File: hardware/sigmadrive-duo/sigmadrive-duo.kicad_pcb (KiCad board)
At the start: 4 copper layers, 100 x 104 mm, 192 parts, among them J10 Conn_01x03, J11 Conn_01x03, J12 Conn_02x05_Odd_Even, J2 CONN_02X05, J4 Conn_01x05, J6 629_105_150_921, J8 Conn_01x03, J9 Conn_01x03, M1 Conn_01x04, M2 Conn_01x04, Q1 NTMFS5C628NLT1G, Q10 NTMFS5C628NLT1G, Q11 NTMFS5C628NLT1G, Q12 NTMFS5C628NLT1G, Q2 NTMFS5C628NLT1G, Q3 NTMFS5C628NLT1G, Q4 NTMFS5C628NLT1G, Q5 NTMFS5C628NLT1G, Q6 NTMFS5C628NLT1G, Q7 NTMFS5C628NLT1G, Q8 NTMFS5C628NLT1G, Q9 NTMFS5C628NLT1G, SW1 SW_DIP_x04, SW2 SW_DIP_x04, U1 DRV8323RS, U12 SN65HVD75DGKR, U2 DRV8323RS, U3 SN65HVD75DGKR, U4 TPD4S009, U5 STM32F745VGTx, U6 TPD4S009, U7 TPS70933, Y1 NX3225SA-12.000M-STD-CSR-1

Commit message: Work on duo drive.
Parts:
- removed R11, R12: 21, Resistor_SMD:R_0603_1608Metric
- removed R6: 10k, Resistor_SMD:R_0603_1608Metric
- removed SW1: SW_DIP_x04, Button_Switch_SMD:SW_DIP_SPSTx04_Slide_Copal_CHS-04A_W5.08mm_P1.27mm_JPin
- added C4: 100nF 50V, Capacitor_SMD:C_0603_1608Metric, F.Cu at (73.2, 104.8)
- added J1: Conn_02x05_Odd_Even, Connector_PinHeader_2.00mm:PinHeader_2x05_P2.00mm_Horizontal, F.Cu at (66.9, 105.0)
- added R10: 10k, Resistor_SMD:R_0603_1608Metric, F.Cu at (70.4, 93.3)
- added R25: 10k, Resistor_SMD:R_0603_1608Metric, F.Cu at (174.6, 93.0)
- added R33: 10k, Resistor_SMD:R_0603_1608Metric, F.Cu at (171.0, 119.9)
- added R48: 10k, Resistor_SMD:R_0603_1608Metric, F.Cu at (182.8, 122.2)
- added R9: 10k, Resistor_SMD:R_0603_1608Metric, F.Cu at (72.6, 93.3)
- added U8: SN65HVD75DGKR, Package_SO:SOIC-8_3.9x4.9mm_P1.27mm, F.Cu at (71.2, 99.2)
- C5, R14, R15, U3: moved to F.Cu
- moved R44 106.4 mm to (136.5, 65.1)
- moved R2 95.5 mm to (121.0, 64.7)
- moved R3 95.5 mm to (122.5, 64.7)
- moved R5 95.5 mm to (124.0, 64.7)
- moved R24 92.5 mm to (106.6, 105.3), turned to 90 degrees
- moved C45 91.1 mm to (103.6, 105.3), turned to 270 degrees
- moved R23 90.3 mm to (108.1, 105.3), turned to 90 degrees
- moved R34 89.7 mm to (105.1, 105.3), turned to 270 degrees
- moved R19 69.5 mm to (98.3, 73.9), turned to 180 degrees
- moved J2 63.1 mm to (126.7, 59.6)
- moved R8 58.2 mm to (127.0, 64.7), turned to 90 degrees
- moved C3 56.9 mm to (125.5, 64.7), turned to 270 degrees
- moved J12 52.9 mm to (148.1, 97.0)
- moved R36 41.3 mm to (221.2, 130.3)
- moved RV2 41.3 mm to (225.8, 130.3)
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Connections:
- C51 pad 2: /MCU/PB14 -> /MCU/SW1
- C52 pad 2: /MCU/PB15 -> /MCU/SW2
- J4 pad 3: /MCU/PB4 -> /MCU/PWM_IN
- J8 pad 3: /MCU/PB14 -> /MCU/SW1
- J9 pad 3: /MCU/PB15 -> /MCU/SW2
- R17 pad 2: /MCU/PB14 -> /MCU/SW1
- R28 pad 2: /MCU/PB15 -> /MCU/SW2
- R36 pad 2: /MCU/PA4 -> /MCU/PC4
- R84 pad 2: /MCU/PD6 -> /MCU/PC11
- R85 pad 1: /MCU/PD4 -> /MCU/PA15
- RV2 pad 2: /MCU/PA4 -> /MCU/PC4
- SW2 pad 2: +3V3 -> GND
- SW2 pad 3: GND -> +3V3
- SW2 pad 5: /MCU/GPIO_CONF_4 -> /MCU/BOOT0
- U1 pad 29: Net-(R12-Pad2) -> /MCU/DRV_SDO
- U12 pad 1: /MCU/PD6 -> /MCU/PC11
- U12 pad 2: /MCU/PD4 -> /MCU/PA15
- U12 pad 3: /MCU/PD4 -> /MCU/PA15
- U12 pad 4: /MCU/PD5 -> /MCU/PC10
- U2 pad 29: Net-(R11-Pad2) -> /MCU/DRV_SDO
- U3 pad 6: Net-(J12-Pad7) -> Net-(J12-Pad5)
- U3 pad 7: Net-(J12-Pad5) -> Net-(J12-Pad7)
- U5 pad 1: /MCU/GPIO_CONF_3 -> /MCU/PE2
- U5 pad 2: /MCU/GPIO_CONF_4 -> /MCU/PE3
- U5 pad 29: /MCU/PA5 -> /MCU/M2_AL
- U5 pad 30: /MCU/PA6 -> /MCU/M2_QUAD_A
- U5 pad 31: /MCU/M2_AL -> /MCU/M2_QUAD_B
- U5 pad 37: /MCU/PE7 -> /MCU/M2_QUAD_Z
- U5 pad 44: /MCU/GATE1_ENABLE -> /MCU/DRV_CAL
- U5 pad 45: /MCU/DRV_CAL -> /MCU/GATE1_ENABLE
- U5 pad 46: /MCU/PB10 -> /MCU/DRV_CLK
- U5 pad 53: /MCU/PB14 -> /MCU/DRV_SDO
- U5 pad 54: /MCU/PB15 -> /MCU/DRV_SDI
- U5 pad 78: /MCU/DRV_CLK -> /MCU/PC10
- U5 pad 79: /MCU/DRV_SDO -> /MCU/PC11
- U5 pad 80: /MCU/DRV_SDI -> /MCU/PC12
- U5 pad 85: /MCU/PD4 -> /MCU/M1_ENCODER_DE
- U5 pad 86: /MCU/PD5 -> /MCU/M1_ENCODER_DI
- U5 pad 87: /MCU/PD6 -> /MCU/M1_ENCODER_RO
- U5 pad 88: /MCU/M2_QUAD_Z -> /MCU/M1_QUAD_Z
- U5 pad 91: /MCU/DIR -> /MCU/PB5
- U5 pad 92: /MCU/M2_QUAD_A -> /MCU/M1_QUAD_A
- U5 pad 93: /MCU/M2_QUAD_B -> /MCU/M1_QUAD_B
- U5 pad 97: /MCU/GPIO_CONF_1 -> /MCU/PE0
- U5 pad 98: /MCU/GPIO_CONF_2 -> /MCU/PE1
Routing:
- net /MCU/DRV_SDO: track 13.6 -> 103.2 mm, vias 0 -> 2
- net /MCU/M1_QUAD_Z: track 0.00 -> 64.5 mm, vias 0 -> 1
- net /MCU/M1_QUAD_B: track 0.00 -> 64.4 mm, vias 0 -> 1
- net /MCU/M1_QUAD_A: track 0.00 -> 64.1 mm, vias 0 -> 1
- net /MCU/M1_ENCODER_DI: track 0.00 -> 63.8 mm
- net /MCU/M1_ENCODER_DE: track 0.00 -> 61.0 mm
- net Net-(R12-Pad2): track 60.5 -> 0.00 mm, vias 5 -> 0
- net Net-(R11-Pad2): track 60.2 -> 0.00 mm, vias 4 -> 0
- net /MCU/M1_ENCODER_RO: track 0.00 -> 55.8 mm
- net /MCU/M2_QUAD_Z: track 0.00 -> 40.5 mm, vias 0 -> 1
- net /MCU/M2_QUAD_A: track 0.00 -> 39.5 mm, vias 0 -> 1
- net /MCU/M2_ENCODER_RO: track 1.81 -> 41.2 mm
- net /MCU/M2_QUAD_B: track 0.00 -> 38.9 mm, vias 0 -> 1
- net /MCU/PC2: track 69.6 -> 35.2 mm, vias 2 -> 0
- net /MCU/PC1: track 67.1 -> 34.4 mm, vias 2 -> 0
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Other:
- board text removed: "BOOT_0"
- board text removed: "CONF_1"
- board text removed: "CONF_2"
- board text removed: "CONF_3"

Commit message: Work on duo drive.
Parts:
- removed J10, J11, J8, J9: Conn_01x03, Connector_PinHeader_2.54mm:PinHeader_1x03_P2.54mm_Horizontal
- added C65: 100nF 50V, Capacitor_SMD:C_0603_1608Metric, F.Cu at (133.0, 79.7)
- added C66: 100nF 50V, Capacitor_SMD:C_0603_1608Metric, F.Cu at (133.0, 74.1)
- added ENC2: Conn_02x05_Odd_Even, Connector_PinHeader_2.00mm:PinHeader_2x05_P2.00mm_Horizontal, F.Cu at (72.0, 94.6)
- added GPIO1: Conn_02x05_Odd_Even, Connector_PinHeader_2.00mm:PinHeader_2x05_P2.00mm_Horizontal, F.Cu at (72.4, 70.3)
- added J3: Conn_02x03_Odd_Even, Connector_PinHeader_2.00mm:PinHeader_2x03_P2.00mm_Horizontal, F.Cu at (85.7, 70.3)
- added J5: Conn_02x03_Odd_Even, Connector_PinHeader_2.00mm:PinHeader_2x03_P2.00mm_Horizontal, F.Cu at (93.6, 70.3)
- added M1_SW1: CONN_02X02, Connector_PinHeader_2.00mm:PinHeader_2x02_P2.00mm_Horizontal, F.Cu at (138.8, 80.0)
- added M1_SW2: CONN_02X02, Connector_PinHeader_2.00mm:PinHeader_2x02_P2.00mm_Horizontal, F.Cu at (138.8, 74.1)
- added M2_SW1: CONN_02X02, Connector_PinHeader_2.00mm:PinHeader_2x02_P2.00mm_Horizontal, F.Cu at (72.0, 82.0)
- added M2_SW2: CONN_02X02, Connector_PinHeader_2.00mm:PinHeader_2x02_P2.00mm_Horizontal, F.Cu at (72.0, 76.1)
- added R11: 100, Resistor_SMD:R_0603_1608Metric, F.Cu at (134.5, 79.7)
- added R12: 10k, Resistor_SMD:R_0603_1608Metric, F.Cu at (136.0, 74.1)
- added R49: 100, Resistor_SMD:R_0603_1608Metric, F.Cu at (134.5, 74.1)
- added R51: 21, Resistor_SMD:R_0603_1608Metric, F.Cu at (141.7, 110.7)
- added R52: 0, Resistor_SMD:R_0603_1608Metric, F.Cu at (116.3, 95.6)
- added R53: 0, Resistor_SMD:R_0603_1608Metric, F.Cu at (116.3, 97.3)
- added R54: 21, Resistor_SMD:R_0603_1608Metric, F.Cu at (141.8, 69.2)
- added R55: 21, Resistor_SMD:R_0603_1608Metric, F.Cu at (141.8, 70.7)
- added R6: 10k, Resistor_SMD:R_0603_1608Metric, F.Cu at (136.0, 79.7)
- C51, C52, C8, R17, R20, R28, R30, R38, R40, R84, R85, R88, U12: moved to F.Cu
- J1: value Conn_02x05_Odd_Even -> CONN_02X02; footprint Connector_PinHeader_2.00mm:PinHeader_2x05_P2.00mm_Horizontal -> Connector_PinHeader_2.00mm:PinHeader_2x02_P2.00mm_Horizontal
- J4: value Conn_01x05 -> CONN_02X02; footprint Connector_PinHeader_2.54mm:PinHeader_1x05_P2.54mm_Horizontal -> Connector_PinHeader_2.00mm:PinHeader_2x02_P2.00mm_Horizontal
- R35, R36, RV1, RV2: moved to B.Cu
- R37: value 10k -> 21; moved to F.Cu
- moved F1 210.3 mm to (66.9, 153.2)
- moved F3 170.1 mm to (66.9, 153.2)
- moved RV2 130.7 mm to (95.3, 137.3), turned to 270 degrees
- moved R36 127.8 mm to (93.6, 137.3), turned to 270 degrees
- moved C56 117.4 mm to (118.8, 96.4)
- moved U7 113.4 mm to (121.7, 96.4), turned to 180 degrees
- moved D1 112.0 mm to (128.0, 72.7)
- moved C50 110.5 mm to (124.6, 96.4), turned to 90 degrees
- moved R48 109.0 mm to (77.5, 94.1), turned to 90 degrees
- moved SW2 106.8 mm to (87.2, 86.1), turned to 90 degrees
- moved R35 104.3 mm to (127.6, 137.3), turned to 270 degrees
- moved D4 103.7 mm to (128.0, 74.2)
- moved R25 100.1 mm to (74.5, 94.1)
- moved F2 99.9 mm to (140.7, 66.4)
- moved F4 99.9 mm to (140.7, 66.4)
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- renumbered J12 to ENC1
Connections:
- C2 pad 1: +3V3 -> +3.3VA
- C42 pad 1: /MCU/PA0 -> /MCU/PA1
- C43 pad 1: /MCU/PA1 -> /MCU/PA2
- C44 pad 1: /MCU/PA2 -> /MCU/PA3
- C51 pad 2: /MCU/SW1 -> /MCU/M2_SW1
- C52 pad 2: /MCU/SW2 -> /MCU/M2_SW2
- C53 pad 2: +3.3VP -> +3.3VA
- C7 pad 1: +3V3 -> +3.3VA
- J1 pad 2: /MCU/M1_QUAD_B -> /MCU/PE1
- J1 pad 3: Net-(J1-Pad3) -> +5V
- J1 pad 4: /MCU/M1_QUAD_A -> /MCU/PE0
- J2 pad 1: +3V3 -> GND
- J2 pad 3: GND -> +3V3
- J4 pad 2: +5V -> Net-(J4-Pad2)
- J4 pad 3: /MCU/PWM_IN -> +5V
- J4 pad 4: /MCU/DIR -> Net-(J4-Pad4)
- R17 pad 2: /MCU/SW1 -> /MCU/M2_SW1
- R27 pad 1: /MCU/PA0 -> /MCU/PA1
- R28 pad 2: /MCU/SW2 -> /MCU/M2_SW2
- R29 pad 1: /MCU/PA1 -> /MCU/PA2
- R31 pad 1: /MCU/PA2 -> /MCU/PA3
- R37 pad 1: +3V3 -> /MCU/DRV_SDO
- R37 pad 2: /MCU/PD2 -> Net-(R37-Pad2)
- R48 pad 1: +3V3 -> /MCU/M1_QUAD_Z
- R48 pad 2: /MCU/M1_QUAD_Z -> +3V3
- U1 pad 26: +3V3 -> +3.3VA
- U1 pad 29: /MCU/DRV_SDO -> Net-(R51-Pad2)
- U2 pad 26: +3V3 -> +3.3VA
- U2 pad 29: /MCU/DRV_SDO -> Net-(R37-Pad2)
- U5 pad 21: +3.3VP -> +3.3VA
- U5 pad 28: /MCU/PA4 -> /MCU/ADC1_IN4
- U5 pad 29: /MCU/M2_AL -> /MCU/PA5
- U5 pad 30: /MCU/M2_QUAD_A -> /MCU/ADC1_IN6
- U5 pad 31: /MCU/M2_QUAD_B -> /MCU/M2_AL
- U5 pad 37: /MCU/M2_QUAD_Z -> /MCU/PE7
- U5 pad 47: /MCU/PB11 -> /MCU/M2_QUAD_Z
- U5 pad 57: /MCU/PD10 -> /MCU/M1_SW1
- U5 pad 58: /MCU/PD11 -> /MCU/M1_SW2
- U5 pad 83: /MCU/PD2 -> /MCU/M2_SW2
- U5 pad 84: /MCU/PD3 -> /MCU/M2_SW1
- U5 pad 90: /MCU/PB4 -> /MCU/M2_QUAD_A
- U5 pad 91: /MCU/PB5 -> /MCU/M2_QUAD_B
- U8 pad 6: Net-(J1-Pad5) -> Net-(ENC2-Pad5)
- U8 pad 7: Net-(J1-Pad7) -> Net-(ENC2-Pad7)
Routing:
- net +3V3: track 28.9 -> 324.8 mm, vias 1 -> 20
- net +5V: track 6.43 -> 198.8 mm, vias 0 -> 3
- net GND: track 38.7 -> 190.4 mm, vias 11 -> 50
- net VIN: track 92.1 -> 177.2 mm, vias 0 -> 111
- net +3.3VA: track 0.00 -> 82.3 mm, vias 0 -> 5
- net /MCU/PC4: track 0.00 -> 71.2 mm, vias 0 -> 3
- net /MCU/PC5: track 0.00 -> 68.2 mm, vias 0 -> 3
- net /MCU/DRV_SDO: track 103.2 -> 43.2 mm, vias 2 -> 0
- net +3.3VP: track 36.2 -> 95.5 mm, vias 0 -> 5
- net Net-(R51-Pad2): track 0.00 -> 58.1 mm, vias 0 -> 2
- net /MCU/ADC1_IN6: track 0.00 -> 56.4 mm, vias 0 -> 1
- net /MCU/PA5: track 0.00 -> 53.9 mm, vias 0 -> 1
- net /MCU/ADC1_IN4: track 0.00 -> 51.3 mm, vias 0 -> 1
- net /MCU/M2_SW2: track 0.00 -> 45.8 mm
- net /MCU/M2_SW1: track 0.00 -> 43.6 mm
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- added copper zone on F.Cu, net +3.3VA
- added copper zone on F.Cu, net +3V3
- added copper zone on F.Cu, net +5V
- added copper zone on B.Cu, net /MOSFETs/M1_A
- added copper zone on In1.Cu, net /MOSFETs/M1_A
- added copper zone on In2.Cu, net /MOSFETs/M1_A
- added copper zone on B.Cu, net /MOSFETs/M1_B
- added copper zone on In1.Cu, net /MOSFETs/M1_B
- added copper zone on In2.Cu, net /MOSFETs/M1_B
- added copper zone on B.Cu, net /MOSFETs/M1_C
- added copper zone on In1.Cu, net /MOSFETs/M1_C
- added copper zone on In2.Cu, net /MOSFETs/M1_C
- added copper zone on B.Cu, net /MOSFETs/M2_A
- added copper zone on In1.Cu, net /MOSFETs/M2_A
- added copper zone on In2.Cu, net /MOSFETs/M2_A
- added copper zone on B.Cu, net /MOSFETs/M2_B
- added copper zone on In1.Cu, net /MOSFETs/M2_B
- added copper zone on In2.Cu, net /MOSFETs/M2_B
- added copper zone on B.Cu, net /MOSFETs/M2_C
- added copper zone on In1.Cu, net /MOSFETs/M2_C
- added copper zone on In2.Cu, net /MOSFETs/M2_C
- added copper zone on B.Cu, net GND
- added copper zone on F.Cu, net GND
- added copper zone on In1.Cu, net GND
- added copper zone on In2.Cu, net GND
- added copper zone on B.Cu, net PGND
- added copper zone on In1.Cu, net PGND
- added copper zone on In2.Cu, net PGND
- added copper zone on B.Cu, net VIN
- added copper zone on In1.Cu, net VIN
- added copper zone on In2.Cu, net VIN
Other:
- board size 100 x 104 mm -> 85 x 100 mm
- board text added: "BOOT_0"
- board text added: "SIGMADRIVE-DUO Ver 3.5"
- board text removed: "CONF_4"
- board text removed: "SIGMADRIVE-SOLO Ver 3.4"

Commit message: Work on duo drive.
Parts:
- added R56: 10k, Resistor_SMD:R_0603_1608Metric, F.Cu at (83.7, 94.1)
- added R57: 10k, Resistor_SMD:R_0603_1608Metric, F.Cu at (139.9, 98.6)
- moved R51 39.3 mm to (104.3, 98.5)
- moved R37 36.5 mm to (105.8, 98.5)
- moved R34 3.85 mm to (108.7, 104.7)
- moved R90 2.82 mm to (139.9, 100.1)
- moved R91 2.82 mm to (139.9, 101.6)
- moved R92 2.82 mm to (139.9, 103.1)
- moved ENC1 1.49 mm to (139.9, 87.6)
- moved ENC2 1.49 mm to (70.9, 95.6)
- moved M1_SW1 1.25 mm to (139.9, 80.6)
- moved M2_SW1 1.25 mm to (70.9, 82.6)
- moved GPIO1 1.10 mm to (72.4, 69.2)
- moved J1 1.10 mm to (103.8, 69.2)
- moved J3 1.10 mm to (85.7, 69.2)
- moved J4 1.10 mm to (136.3, 69.2)
- moved J5 1.10 mm to (93.6, 69.2)
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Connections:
- ENC1 pad 8: Net-(ENC1-Pad8) -> /MCU/M2_TIM_CH3
- ENC2 pad 8: Net-(ENC2-Pad8) -> /MCU/M1_TIM_CH3
- GPIO1 pad 2: /MCU/ADC1_IN6 -> /MCU/PB9
- U5 pad 18: /MCU/VBAT_ADC -> /MCU/DRV_SDO
- U5 pad 30: /MCU/ADC1_IN6 -> /MCU/VBAT_ADC
- U5 pad 34: /MCU/M2_BL -> /MCU/M2_TIM_CH3
- U5 pad 53: /MCU/DRV_SDO -> /MCU/M2_BL
- U5 pad 95: /MCU/PB8 -> /MCU/M1_TIM_CH3
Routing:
- net /MCU/M1_TIM_CH3: track 0.00 -> 66.4 mm, vias 0 -> 2
- net Net-(R37-Pad2): track 8.79 -> 73.4 mm, vias 0 -> 2
- net /MCU/ADC1_IN6: track 56.4 -> 0.00 mm, vias 1 -> 0
- net /MCU/PB9: track 0.00 -> 44.4 mm, vias 0 -> 1
- net /MCU/M2_TIM_CH3: track 0.00 -> 37.5 mm, vias 0 -> 2
- net Net-(R51-Pad2): track 58.1 -> 22.3 mm
- net /MCU/DRV_SDO: track 43.2 -> 13.2 mm
- net +5V: track 198.8 -> 211.8 mm
- net /MCU/M2_BL: track 42.6 -> 51.9 mm
- net /MCU/VBAT_ADC: track 21.7 -> 29.5 mm, vias 0 -> 2
- net VIN: track 177.2 -> 171.8 mm, vias 111 -> 112
- net +3.3VA: track 82.3 -> 86.2 mm
- net /MCU/M2_QUAD_Z: track 30.7 -> 34.4 mm
- net /MCU/DRV_FAULT: track 101.2 -> 98.0 mm
- net /MCU/M1_QUAD_A: track 58.1 -> 61.1 mm
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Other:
- outline, holes or cut-outs redrawn

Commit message: Sigmadrive-duo final HW update
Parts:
- R88: value 100 -> 120
- moved R35 1.80 mm to (125.8, 136.5), turned to 90 degrees
- moved RV1 1.60 mm to (127.5, 136.5)
- moved J5 0.60 mm to (94.2, 69.2)
- moved C36 0.30 mm to (69.9, 137.0)
- moved C37 0.30 mm to (69.9, 126.0)
- moved Q5 0.20 mm to (112.5, 138.2)
- moved Q7 0.20 mm to (79.5, 138.2)
- turned U4 to 0 degrees
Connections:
- C44 pad 1: /MCU/PA3 -> /MCU/PA4
- C58 pad 1: /MCU/PC2 -> /MCU/PC3
- GPIO1 pad 6: /MCU/ADC1_IN4 -> /MCU/ADC3_IN3
- R31 pad 1: /MCU/PA3 -> /MCU/PA4
- R43 pad 1: /MCU/PC2 -> /MCU/PC3
- U4 pad 1: /MCU/M1_IA_FB -> /MCU/M1_IC_FB
- U4 pad 10: /MCU/M1_IA_FB -> /MCU/M1_IC_FB
- U4 pad 4: /MCU/M1_IC_FB -> /MCU/M1_IA_FB
- U4 pad 7: /MCU/M1_IC_FB -> /MCU/M1_IA_FB
- U5 pad 17: /MCU/PC2 -> /MCU/DRV_SDO
- U5 pad 18: /MCU/DRV_SDO -> /MCU/PC3
- U5 pad 25: /MCU/PA3 -> /MCU/ADC3_IN3
- U5 pad 28: /MCU/ADC1_IN4 -> /MCU/PA4
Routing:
- net /MCU/ADC1_IN4: track 51.1 -> 0.00 mm, vias 1 -> 0
- net /MCU/ADC3_IN3: track 0.00 -> 50.2 mm, vias 0 -> 1
- net /MCU/PC2: track 35.8 -> 0.00 mm
- net /MCU/PC3: track 0.00 -> 35.6 mm
- net /MCU/PA4: track 0.00 -> 30.6 mm, vias 0 -> 2
- net /MCU/PA3: track 26.0 -> 0.00 mm
- net /MCU/DRV_SDO: track 13.2 -> 17.5 mm, vias 0 -> 2
- net /MCU/M1_CH: track 33.1 -> 36.6 mm, vias 0 -> 2
- net /MCU/M2_TIM_CH3: track 37.5 -> 40.6 mm, vias 2 -> 1
- net /MCU/M1_CL: track 32.7 -> 35.7 mm, vias 0 -> 2
- net /MCU/PC5: track 67.9 -> 66.1 mm
- net /MCU/M1_TIM_CH3: track 66.4 -> 67.8 mm
- net +5V: track 211.8 -> 213.0 mm, vias 3 -> 4
- net +3V3: track 325.3 -> 326.6 mm
- net /MCU/DRV_FAULT: track 98.0 -> 96.9 mm
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
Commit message: PCB sigmadrive-duo, version 3.6
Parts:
- removed FB2: 0.6OHM/0.2A/2.2 kOhm, Resistor_SMD:R_0603_1608Metric
- added C67: 10uF 35V, Capacitor_SMD:C_0805_2012Metric, F.Cu at (119.6, 103.0)
- C26, C35, C47, C48: footprint Capacitor_SMD:C_1206_3216Metric -> Capacitor_SMD:C_0805_2012Metric
- C46: value 4.7uF 50V -> 10uF 35V
- M1, M2: value Conn_01x04 -> Conn_01x03; footprint Connector_Molex:Molex_Micro-Fit_3.0_43650-0400_1x04_P3.00mm_Horizontal -> Connector_Molex:Molex_Micro-Fit_3.0_43650-0300_1x03_P3.00mm_Horizontal
- R37, R51: value 21 -> 10k
- R52: value 0 -> N/A
- moved C46 15.7 mm to (79.4, 103.0)
- moved C49 15.2 mm to (99.9, 88.7), turned to 180 degrees
- moved M1 3.20 mm to (132.4, 152.3)
- moved M2 3.20 mm to (99.4, 152.3)
- moved D6 2.47 mm to (76.7, 102.8)
- moved R21 2.47 mm to (75.2, 102.8)
- moved C27 1.63 mm to (92.8, 90.5)
- moved C32 1.63 mm to (92.8, 93.0)
- moved Y1 1.63 mm to (96.2, 91.8)
- moved C47 0.40 mm to (121.5, 103.0)
- moved FB1 0.40 mm to (109.2, 98.9)
- moved R37 0.40 mm to (105.8, 98.9), turned to 90 degrees
- moved R51 0.40 mm to (104.3, 98.9), turned to 90 degrees
- moved C48 0.30 mm to (81.4, 103.0)
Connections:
- net /MCU/M1_ENCODER_DE renamed /MCU/ENCODER_DE_M2
- net /MCU/M1_ENCODER_DI renamed /MCU/ENCODER_DI_M2
- net /MCU/M1_ENCODER_RO renamed /MCU/ENCODER_RO_M2
- net /MCU/M1_QUAD_A renamed /MCU/PB6
- net /MCU/M1_QUAD_B renamed /MCU/PB7
- net /MCU/M1_QUAD_Z renamed /MCU/PD7
- net /MCU/M1_TIM_CH3 renamed /MCU/PB8
- net /MCU/M2_ENCODER_DE renamed /MCU/ENCODER_DE_M1
- net /MCU/M2_ENCODER_DI renamed /MCU/ENCODER_DI_M1
- net /MCU/M2_ENCODER_RO renamed /MCU/ENCODER_RO_M1
- net /MCU/M2_QUAD_A renamed /MCU/PB4
- net /MCU/M2_QUAD_B renamed /MCU/PB5
- net /MCU/M2_QUAD_Z renamed /MCU/PB11
- net /MCU/M2_TIM_CH3 renamed /MCU/PB0
- C14 pad 2: +3.3VP -> +3V3
- C19 pad 2: +3.3VP -> +3V3
- C24 pad 2: +3.3VP -> +3V3
- C28 pad 1: +3.3VP -> +3V3
- C46 pad 1: +3.3VP -> +3V3
- C49 pad 1: +3.3VP -> +3V3
- C54 pad 2: +3.3VP -> +3V3
- C55 pad 2: +3.3VP -> +3V3
- J2 pad 1: GND -> +3V3
- J2 pad 3: +3V3 -> GND
- M1 pad 1: PGND -> /MOSFETs/M1_C
- M1 pad 2: /MOSFETs/M1_C -> /MOSFETs/M1_B
- M1 pad 3: /MOSFETs/M1_B -> /MOSFETs/M1_A
- M2 pad 1: PGND -> /MOSFETs/M2_C
- M2 pad 2: /MOSFETs/M2_C -> /MOSFETs/M2_B
- M2 pad 3: /MOSFETs/M2_B -> /MOSFETs/M2_A
- R37 pad 1: /MCU/DRV_SDO -> +3V3
- R37 pad 2: Net-(R37-Pad2) -> /MCU/DRV_SDO
- R51 pad 1: /MCU/DRV_SDO -> +3V3
- R51 pad 2: Net-(R51-Pad2) -> /MCU/DRV_FAULT
- U1 pad 29: Net-(R51-Pad2) -> /MCU/DRV_SDO
- U2 pad 29: Net-(R37-Pad2) -> /MCU/DRV_SDO
- U5 pad 100: +3.3VP -> +3V3
- U5 pad 11: +3.3VP -> +3V3
- U5 pad 27: +3.3VP -> +3V3
- U5 pad 50: +3.3VP -> +3V3
- U5 pad 6: +3.3VP -> +3V3
- U5 pad 75: +3.3VP -> +3V3
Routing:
- net +3.3VP: track 95.5 -> 0.00 mm, vias 5 -> 0
- net +3V3: track 326.6 -> 417.3 mm, vias 22 -> 24
- net /MCU/DRV_SDO: track 17.5 -> 94.1 mm, vias 2 -> 5
- net Net-(R37-Pad2): track 72.7 -> 0.00 mm, vias 2 -> 0
- net Net-(R51-Pad2): track 22.3 -> 0.00 mm, vias 2 -> 0
- net /MCU/DRV_FAULT: track 96.9 -> 101.4 mm, vias 4 -> 5
- net +5V: track 213.0 -> 216.2 mm
- net Net-(C27-Pad1): track 14.7 -> 16.4 mm
- net Net-(C32-Pad1): track 16.1 -> 17.7 mm
- net Net-(C30-Pad1): track 11.5 -> 12.4 mm
- net GND: track 192.7 -> 192.4 mm, vias 49 -> 62
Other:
- board text added: "SIGMADRIVE-DUO Ver 3.6"
- board text removed: "SIGMADRIVE-DUO Ver 3.5"

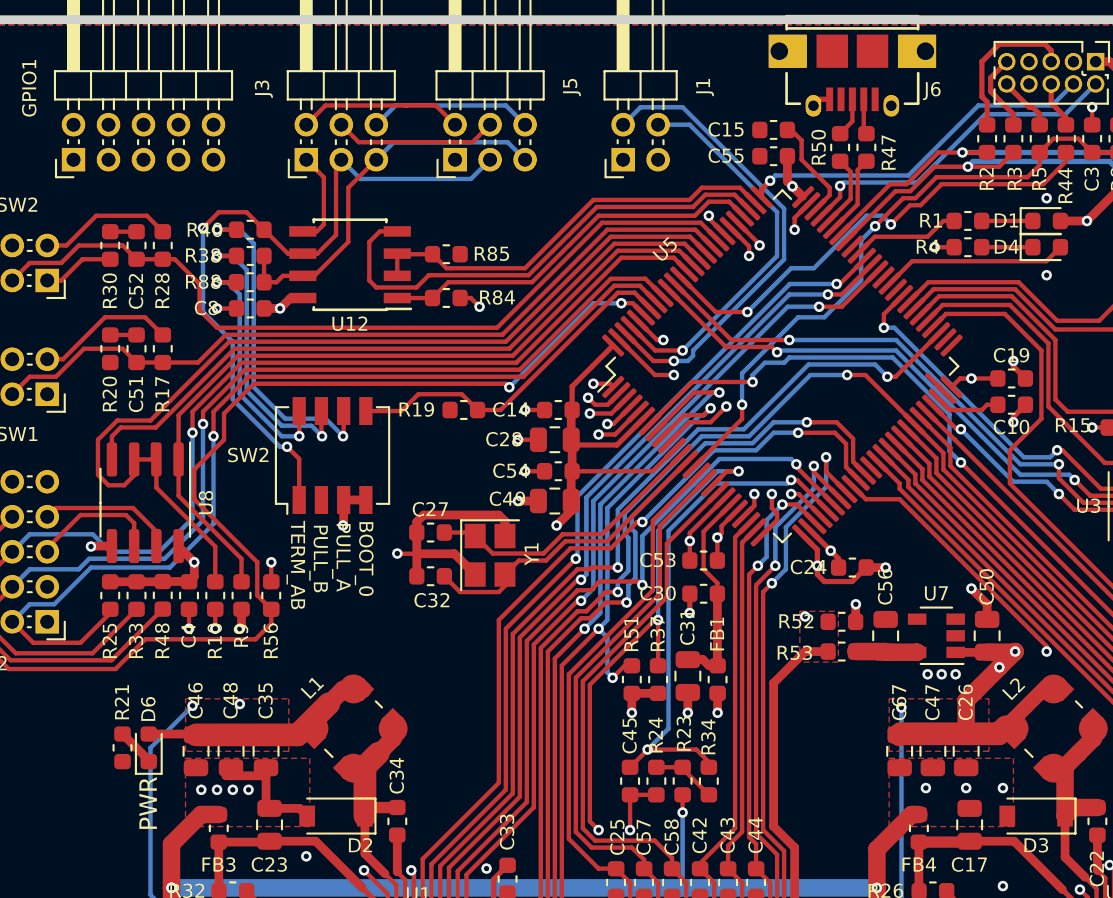
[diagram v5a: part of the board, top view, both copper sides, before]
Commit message: Added more ground vias.
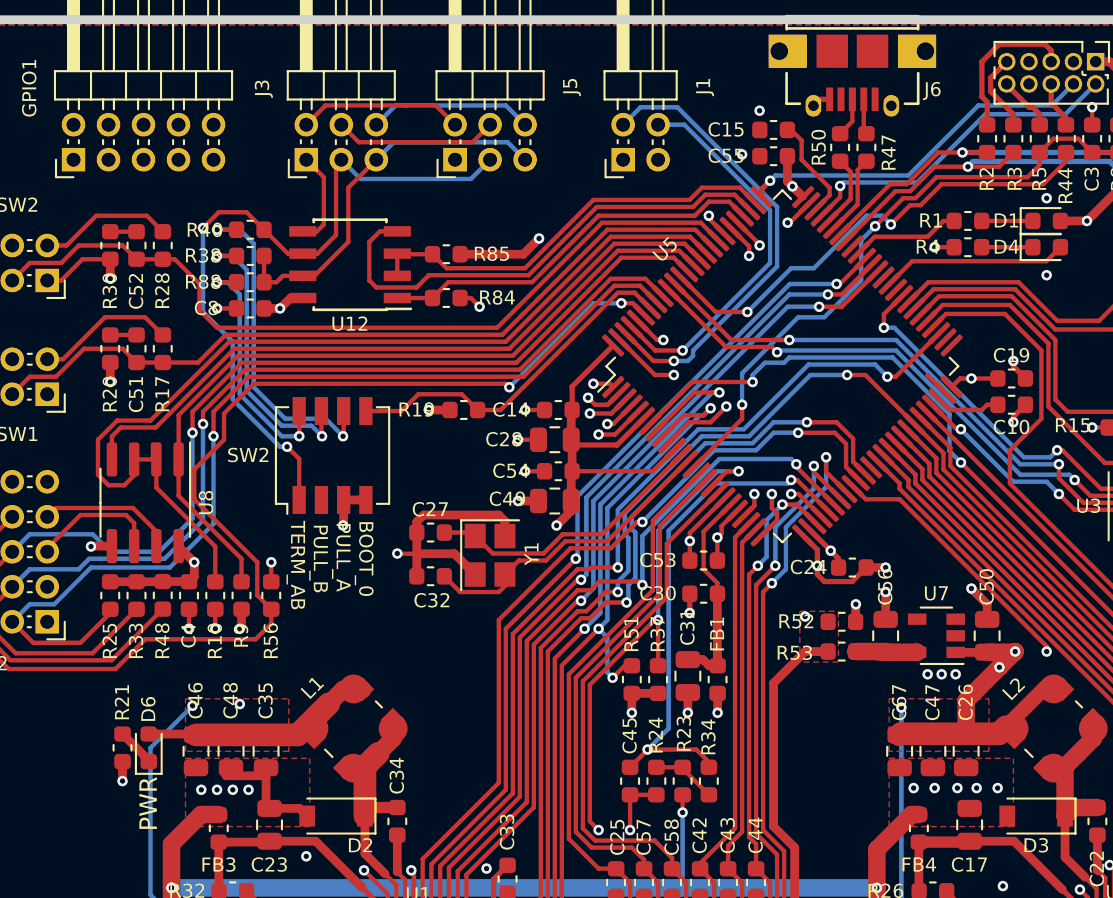
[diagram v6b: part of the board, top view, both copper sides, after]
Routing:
- net GND: track 192.4 -> 203.2 mm, vias 62 -> 72
- net /MCU/PE1: track 27.2 -> 26.7 mm
- net /MCU/PE0: track 22.5 -> 22.0 mm
